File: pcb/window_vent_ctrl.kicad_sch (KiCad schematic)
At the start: 32 parts, among them J1 12V IN, J2 FAN 0 intake, J3 FAN 1 exhaust, J4 MOTOR, J5 SCD40, J6 AS5600, J7 DS18B20 in, J8 DS18B20 out, U1 Freenove ESP32-S3 Lite, U2 TMC2209 module

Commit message: Controller PCB v1.1: solder jumper JP2 joins GPIO 21 to GPIO 3 (audio mode)
JP2, open by default, on the back under the ESP32: bridge it to read a
microphone on J7 with GPIO 3 (ADC1). The board is re-routed; the routing
now keeps vias off every silkscreen label. The v1.0 Gerber zip stays (the
boards already ordered). Docs, Pins.h and the wiring diagram mention JP2.

Co-Authored-By: Claude Opus 5.5 <noreply@anthropic.com>
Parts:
- added JP2: AUDIO, Jumper:SolderJumper-2_P1.3mm_Open_RoundedPad1.0x1.5mm, symbol Jumper:SolderJumper_2_Open
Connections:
- net DQ_IN: now also JP2.1 (A)
- net MIC: now reaches U1.12 (GPIO3)
- net MIC: now also JP2.2 (B)
- no-connect marks 23 -> 22
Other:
- note added: "JP2 (solder jumper on the back, open): bridge it for the audio mode, a microphone on J7 read on GPIO 3 (GPIO 21 has no ADC); leave R9 out then."
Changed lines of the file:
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@@
 (generator_version "10.0")
 (paper "A3")
-(title_block (title "Window vent controller") (date "2026-10-24") (rev "1.0") (comment 1 "github.com/mmassico/window_air_vent") (comment 2 "Generated by tools/pcb_schematic.py from tools/pcb_parts.py"))
+(title_block (title "Window vent controller") (date "2026-10-29") (rev "1.1") (comment 1 "github.com/mmassico/window_air_vent") (comment 2 "Generated by tools/pcb_schematic.py from tools/pcb_parts.py"))
 (symbol (lib_id "window_vent:ESP32S3_Lite") (at 76.2 116.84 0) (unit 1) (exclude_from_sim no) (in_bom yes) (on_board yes) (dnp no) (property "Reference" "U1" (at 66.04 86.11 0) (effects (font (size 1.27 1.27)) (justify left))) (property "Value" "Freenove ESP32-S3 Lite" (at 66.04 88.31 0) (effects (font (size 1.27 1.27)) (justify left))) (property "Footprint" "window_vent:Freenove_ESP32S3_Lite" (at 76.2 116.84 0) (hide yes) (effects (font (size 1.27 1.27)))) (property "Datasheet" "" (at 76.2 116.84 0) (hide yes) (effects (font (size 1.27 1.27)))) (property "Description" "" (at 76.2 116.84 0) (hide yes) (effects (font (size 1.27 1.27)))) (pin "1") (pin "2") (pin "3") (pin "4") (pin "5") (pin "6") (pin "7") (pin "8") (pin "9") (pin "10") (pin "11") (pin "12") (pin "13") (pin "14") (pin "15") (pin "16") (pin "17") (pin "18") (pin "19") (pin "20") (pin "21") (pin "22") (pin "23") (pin "24") (pin "25") (pin "26") (pin "27") (pin "28") (pin "29") (pin "30") (pin "31") (pin "32") (pin "33") (pin "34") (pin "35") (pin "36") (pin "37") (pin "38") (pin "39") (pin "40") (instances (project "window_vent_ctrl" (path "/6185b689-d256-54e4-b89c-a925e8b04148" (reference "U1") (unit 1)))))
 (wire (pts (xy 60.96 92.71) (xy 58.42 92.71)) (stroke (width 0) (type default)))
@@
 (wire (pts (xy 60.96 118.11) (xy 58.42 118.11)) (stroke (width 0) (type default)))
 (label "SCD_SDA" (at 58.42 118.11 180) (effects (font (size 1.27 1.27)) (justify right bottom)))
-(no_connect (at 60.96 120.65))
+(wire (pts (xy 60.96 120.65) (xy 58.42 120.65)) (stroke (width 0) (type default)))
+(label "MIC" (at 58.42 120.65 180) (effects (font (size 1.27 1.27)) (justify right bottom)))
 (no_connect (at 60.96 123.19))
 (wire (pts (xy 60.96 125.73) (xy 58.42 125.73)) (stroke (width 0) (type default)))
@@
 (wire (pts (xy 325.12 38.1) (xy 327.66 38.1)) (stroke (width 0) (type default)))
 (label "+12V" (at 327.66 38.1 0) (effects (font (size 1.27 1.27)) (justify left bottom)))
+(symbol (lib_id "Jumper:SolderJumper_2_Open") (at 300.99 177.8 0) (unit 1) (exclude_from_sim no) (in_bom no) (on_board yes) (dnp no) (property "Reference" "JP2" (at 303.53 173.2 0) (effects (font (size 1.27 1.27)) (justify left))) (property "Value" "AUDIO" (at 303.53 175.1 0) (effects (font (size 1.27 1.27)) (justify left))) (property "Footprint" "Jumper:SolderJumper-2_P1.3mm_Open_RoundedPad1.0x1.5mm" (at 300.99 177.8 0) (hide yes) (effects (font (size 1.27 1.27)))) (property "Datasheet" "" (at 300.99 177.8 0) (hide yes) (effects (font (size 1.27 1.27)))) (property "Description" "" (at 300.99 177.8 0) (hide yes) (effects (font (size 1.27 1.27)))) (pin "1") (pin "2") (instances (project "window_vent_ctrl" (path "/6185b689-d256-54e4-b89c-a925e8b04148" (reference "JP2") (unit 1)))))
+(wire (pts (xy 295.91 177.8) (xy 293.37 177.8)) (stroke (width 0) (type default)))
+(label "DQ_IN" (at 293.37 177.8 180) (effects (font (size 1.27 1.27)) (justify right bottom)))
+(wire (pts (xy 306.07 177.8) (xy 308.61 177.8)) (stroke (width 0) (type default)))
+(label "MIC" (at 308.61 177.8 0) (effects (font (size 1.27 1.27)) (justify left bottom)))
 (symbol (lib_id "Device:D_Schottky") (at 320.04 50.8 180) (unit 1) (exclude_from_sim no) (in_bom yes) (on_board yes) (dnp no) (property "Reference" "D1" (at 322.58 46.2 0) (effects (font (size 1.27 1.27)) (justify left))) (property "Value" "1N5822" (at 322.58 48.1 0) (effects (font (size 1.27 1.27)) (justify left))) (property "Footprint" "Diode_THT:D_DO-201AD_P5.08mm_Vertical_AnodeUp" (at 320.04 50.8 0) (hide yes) (effects (font (size 1.27 1.27)))) (property "Datasheet" "" (at 320.04 50.8 0) (hide yes) (effects (font (size 1.27 1.27)))) (property "Description" "" (at 320.04 50.8 0) (hide yes) (effects (font (size 1.27 1.27)))) (pin "1") (pin "2") (instances (project "window_vent_ctrl" (path "/6185b689-d256-54e4-b89c-a925e8b04148" (reference "D1") (unit 1)))))
 (wire (pts (xy 323.85 50.8) (xy 326.39 50.8)) (stroke (width 0) (type default)))
@@
 (text "GPIO 38, 39, 40 stay free for the INMP441 microphone reserved in Pins.h (no room for its header on this board)." (exclude_from_sim no) (at 38.1 252.73 0) (effects (font (size 1.524 1.524)) (justify left bottom)))
 (text "AS5600: tie its DIR pin to GND at the module. C1 sits next to U2's VM pin." (exclude_from_sim no) (at 38.1 256.54 0) (effects (font (size 1.524 1.524)) (justify left bottom)))
+(text "JP2 (solder jumper on the back, open): bridge it for the audio mode, a microphone on J7 read on GPIO 3 (GPIO 21 has no ADC); leave R9 out then." (exclude_from_sim no) (at 38.1 260.35 0) (effects (font (size 1.524 1.524)) (justify left bottom)))
 (sheet_instances (path "/" (page "1")))
 )

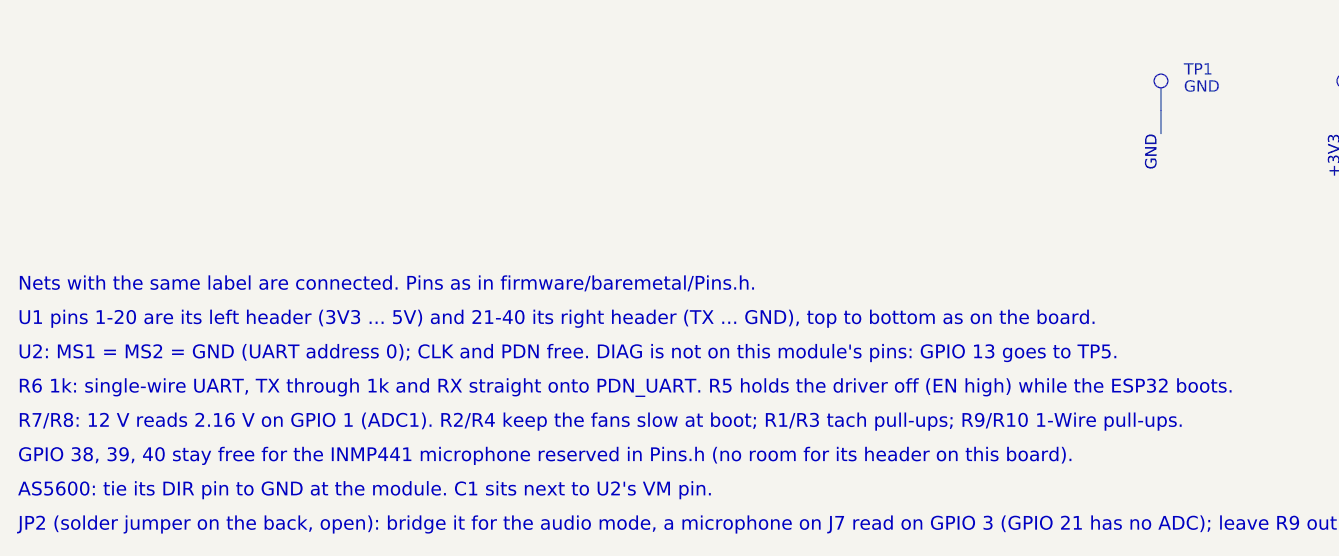
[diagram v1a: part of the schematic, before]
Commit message: Firmware: drivers moved to a shared library (firmware/libs/WindowVent)
The pin map, the drivers and the serial console leave baremetal/ for an
Arduino library, so the coming web application can use them too. Builds
pass --libraries libs; the scripts and the schematic note point at the
new Pins.h path.

Co-Authored-By: Claude Opus 5.5 <noreply@anthropic.com>
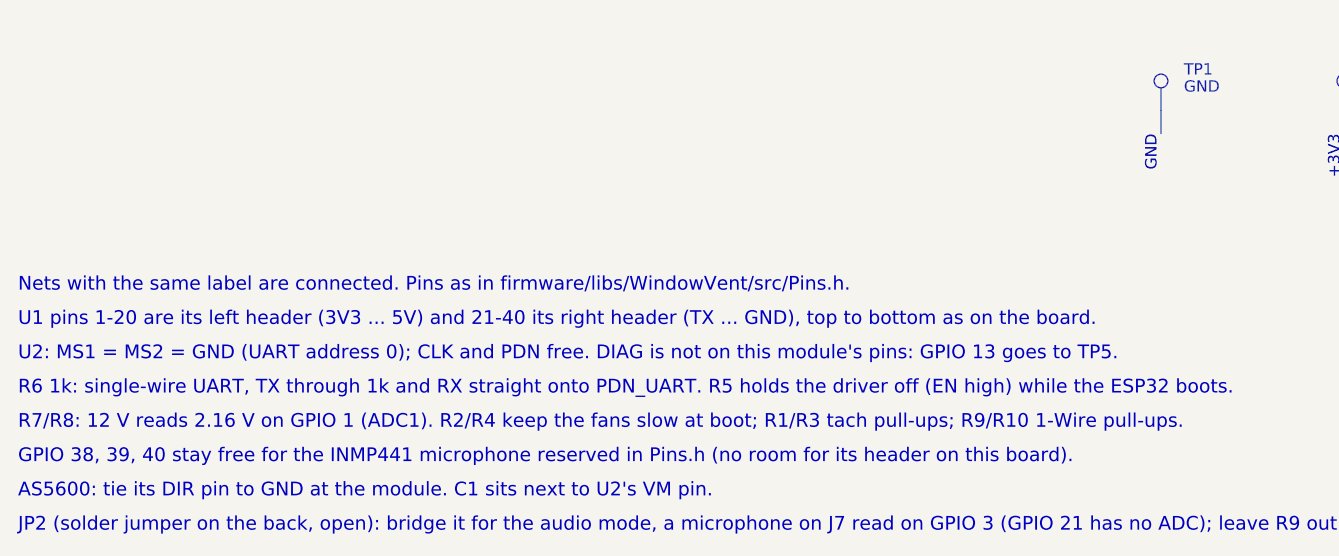
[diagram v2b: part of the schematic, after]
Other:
- note added: "Nets with the same label are connected. Pins as in firmware/libs/WindowVent/src/Pins.h."
- note removed: "Nets with the same label are connected. Pins as in firmware/baremetal/Pins.h."
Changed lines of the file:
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@@
 (text "Test pads" (exclude_from_sim no) (at 157.48 200.66 0) (effects (font (size 1.778 1.778) (bold yes)) (justify left bottom)))
 (text "Mounting holes (M2)" (exclude_from_sim no) (at 233.68 200.66 0) (effects (font (size 1.778 1.778) (bold yes)) (justify left bottom)))
-(text "Nets with the same label are connected. Pins as in firmware/baremetal/Pins.h." (exclude_from_sim no) (at 38.1 233.68 0) (effects (font (size 1.524 1.524)) (justify left bottom)))
+(text "Nets with the same label are connected. Pins as in firmware/libs/WindowVent/src/Pins.h." (exclude_from_sim no) (at 38.1 233.68 0) (effects (font (size 1.524 1.524)) (justify left bottom)))
 (text "U1 pins 1-20 are its left header (3V3 ... 5V) and 21-40 its right header (TX ... GND), top to bottom as on the board." (exclude_from_sim no) (at 38.1 237.49 0) (effects (font (size 1.524 1.524)) (justify left bottom)))
 (text "U2: MS1 = MS2 = GND (UART address 0); CLK and PDN free. DIAG is not on this module's pins: GPIO 13 goes to TP5." (exclude_from_sim no) (at 38.1 241.3 0) (effects (font (size 1.524 1.524)) (justify left bottom)))
